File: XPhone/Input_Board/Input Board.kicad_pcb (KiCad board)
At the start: 2 copper layers, 100 x 100 mm, 94 parts, among them J1 AUDIO, J10 ENV, J11 PULSE, J12 PULSE, J13 Power In, J14 Power Out, J2 AUDIO, J3 ENV, J4 ENV, J5 PULSE, J6 PULSE, J7 AUDIO, J8 AUDIO, J9 ENV, Q1 BC847CW, Q2 BC847CW, Q3 BC847CW, Q4 BC847CW, Q5 BC847CW, Q6 BC847CW, Q7 BC847CW, Q8 BC847CW, U1 LM833, U2 78L05, U3 TL084, U4 74HC14, U5 LM833

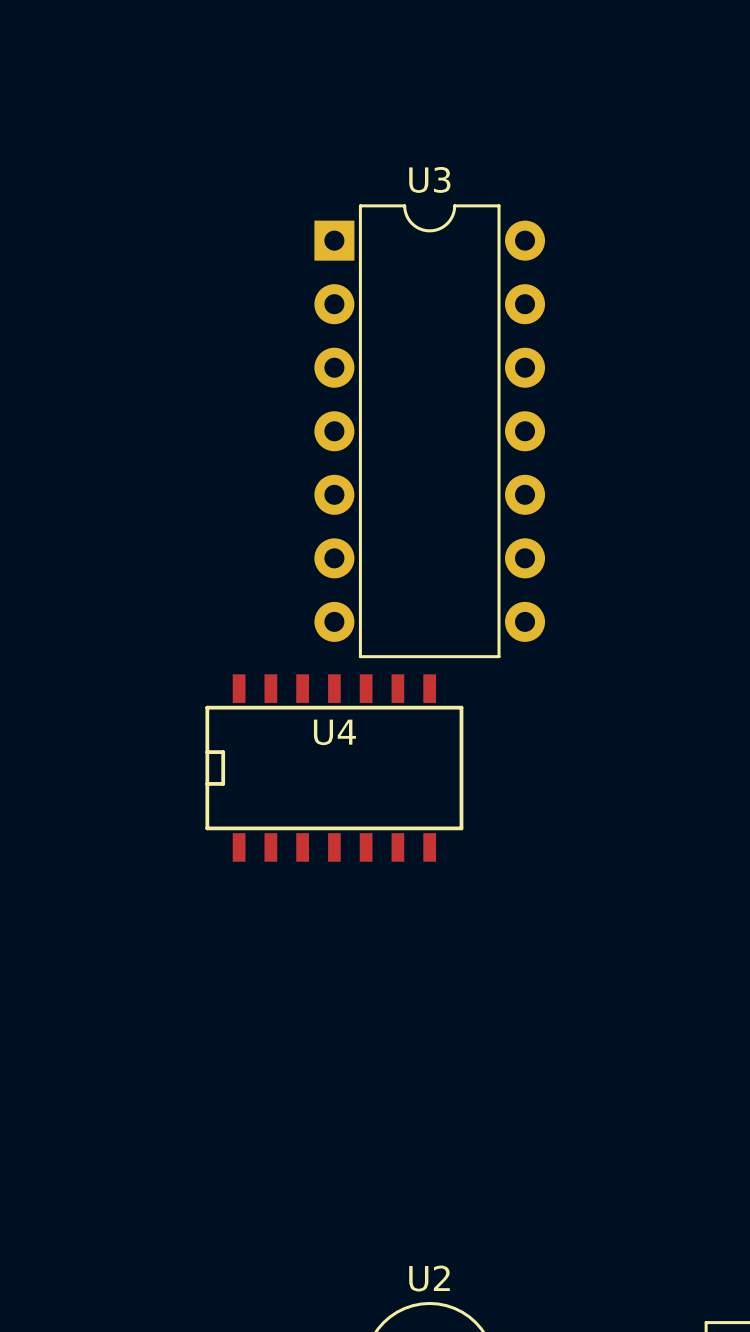
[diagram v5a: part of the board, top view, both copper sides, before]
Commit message: made tl084 a SOIC and returned 74hc14 back to a DIP
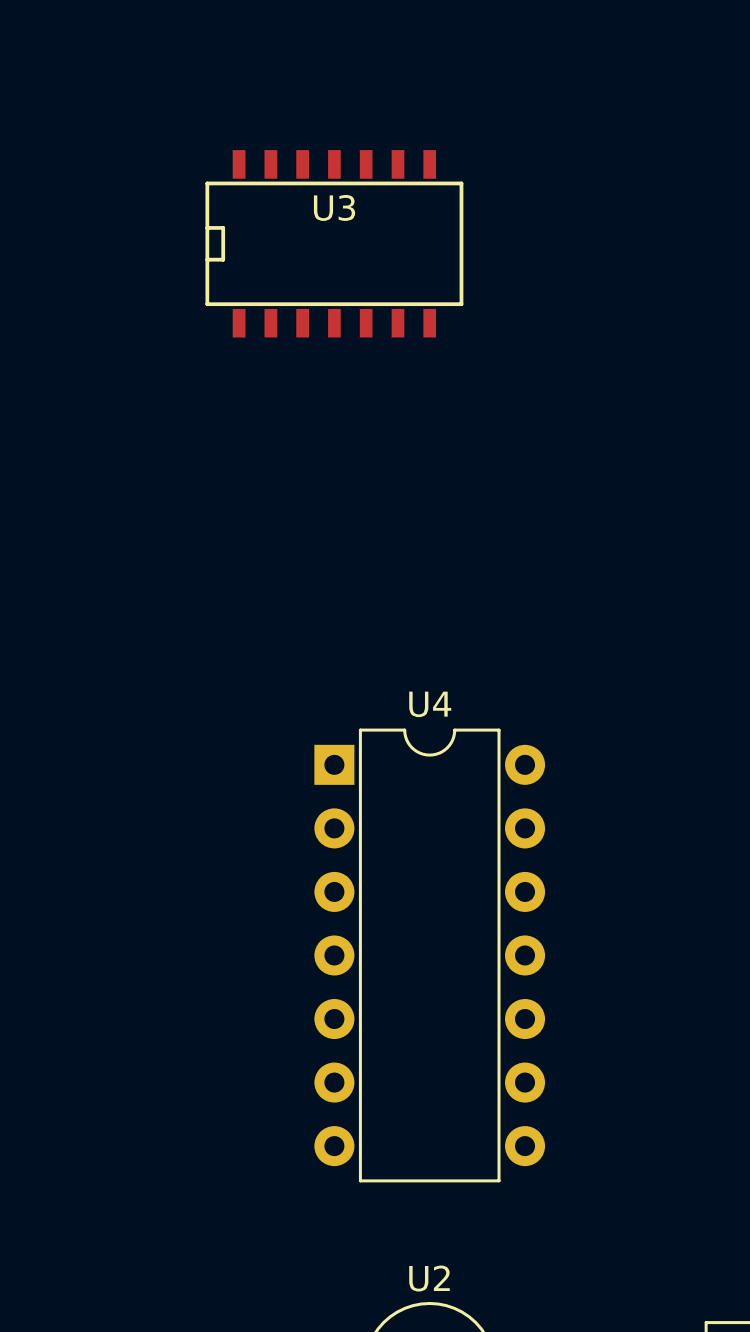
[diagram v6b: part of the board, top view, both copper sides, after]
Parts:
- U3: footprint Housings_DIP:DIP-14_W7.62mm -> SMD_Packages:SOIC-14_N
- U4: footprint SMD_Packages:SOIC-14_N -> Housings_DIP:DIP-14_W7.62mm

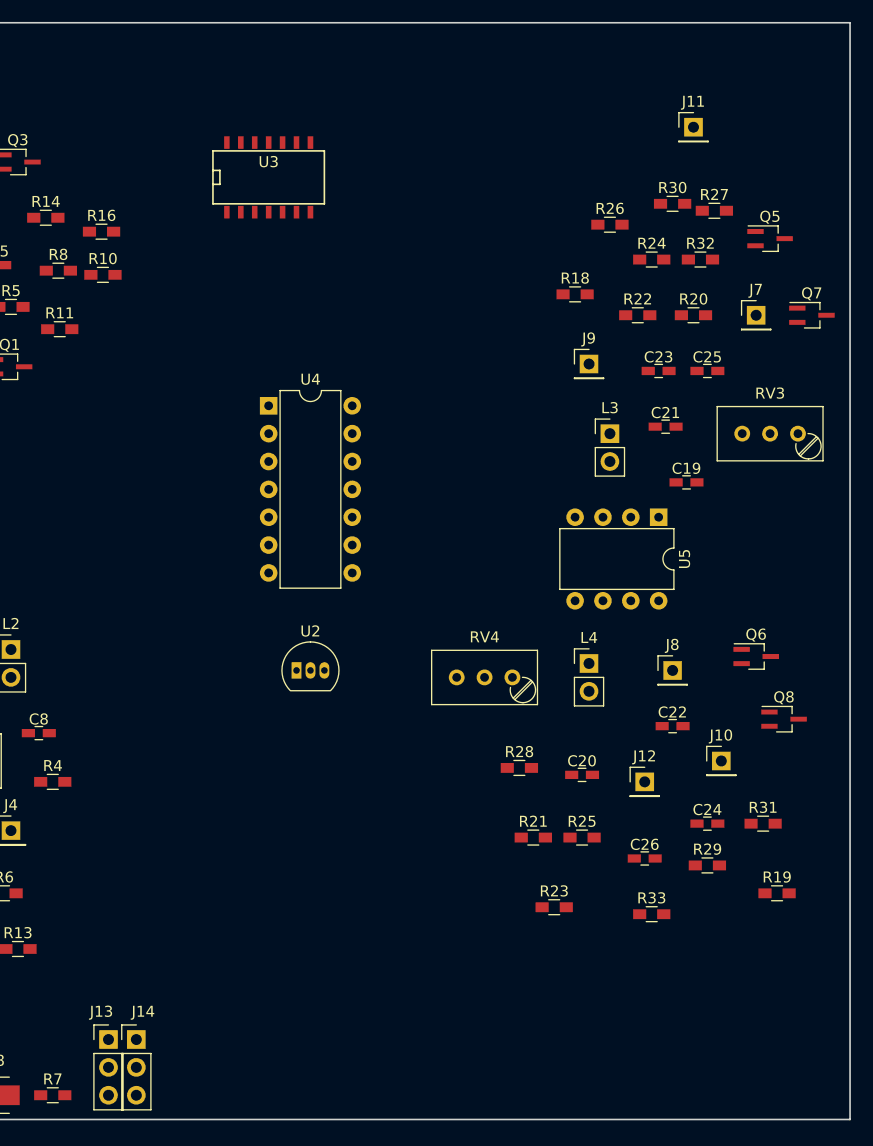
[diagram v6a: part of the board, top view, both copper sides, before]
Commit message: XPhone/Input_Board - placed parts around L3 amplifier
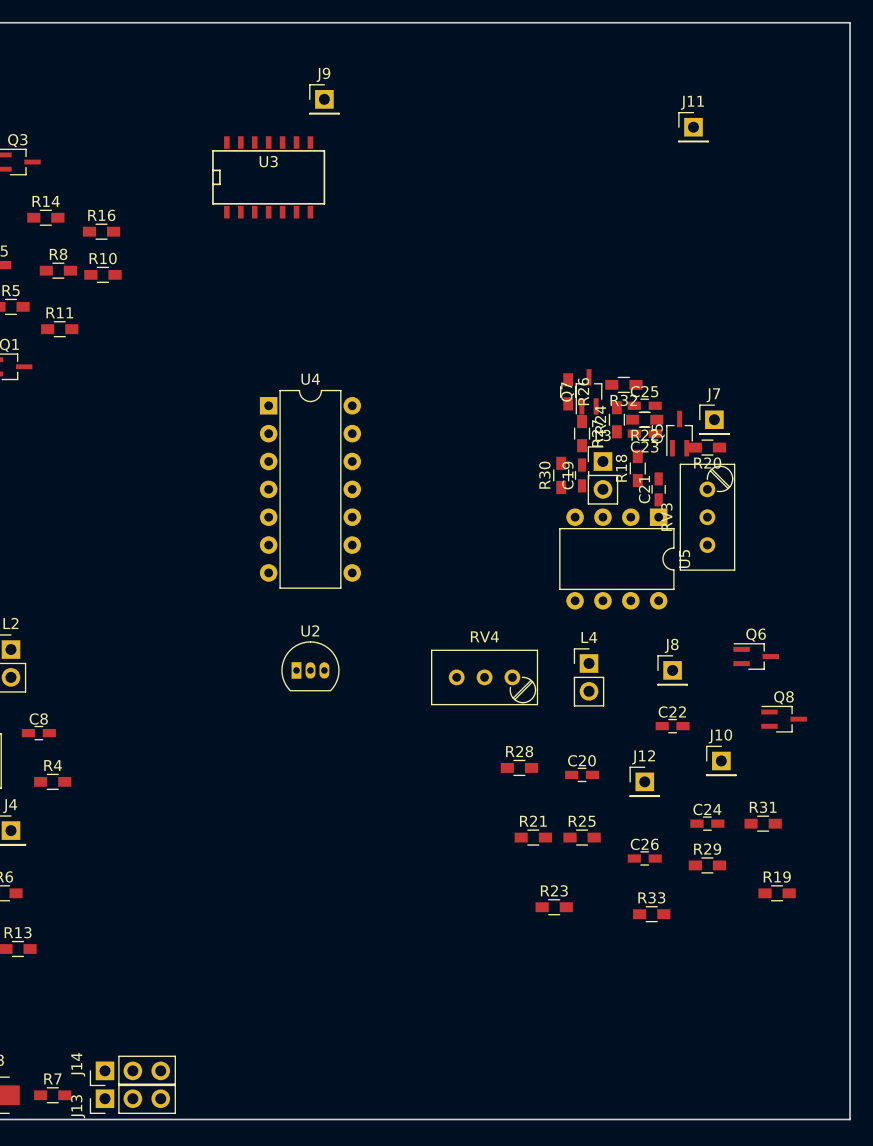
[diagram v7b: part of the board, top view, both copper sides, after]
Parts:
- moved J9 34.1 mm to (62.9, 17.8)
- moved R30 26.8 mm to (84.5, 52.1), turned to 90 degrees
- moved R27 23.6 mm to (86.4, 48.3), turned to 270 degrees
- moved Q7 21.5 mm to (87.0, 44.5), turned to 90 degrees
- moved Q5 19.6 mm to (95.2, 48.3), turned to 90 degrees
- moved R18 16.9 mm to (91.4, 51.4), turned to 90 degrees
- moved R26 15.7 mm to (85.1, 44.5), turned to 270 degrees
- moved R24 14.9 mm to (89.5, 47.0), turned to 90 degrees
- moved R32 13.4 mm to (90.2, 43.8), turned to 180 degrees
- moved R20 12.1 mm to (97.8, 49.5), turned to 180 degrees
- moved J7 10.3 mm to (98.4, 47.0)
- moved RV3 9.69 mm to (97.8, 53.3), turned to 90 degrees
- moved C19 9.55 mm to (86.4, 52.1), turned to 90 degrees
- moved R22 9.55 mm to (92.1, 47.0), turned to 180 degrees
- moved C25 6.54 mm to (92.1, 45.7)
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
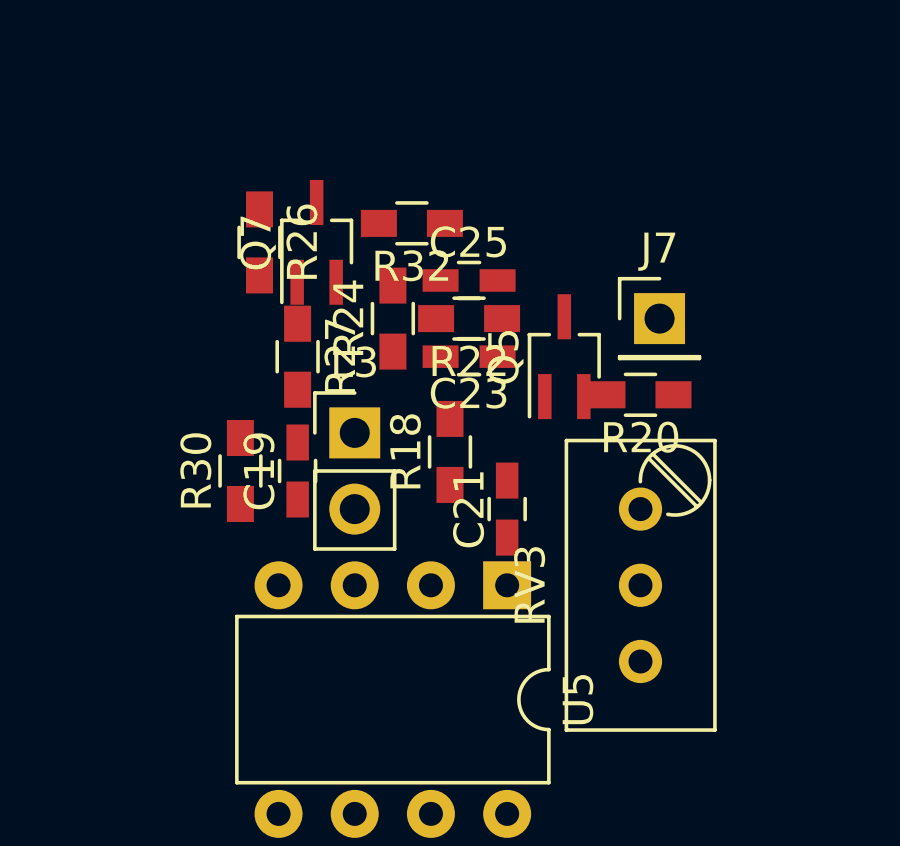
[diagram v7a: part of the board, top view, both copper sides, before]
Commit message: XPhone/Input_Board - laid traces for parts around L3
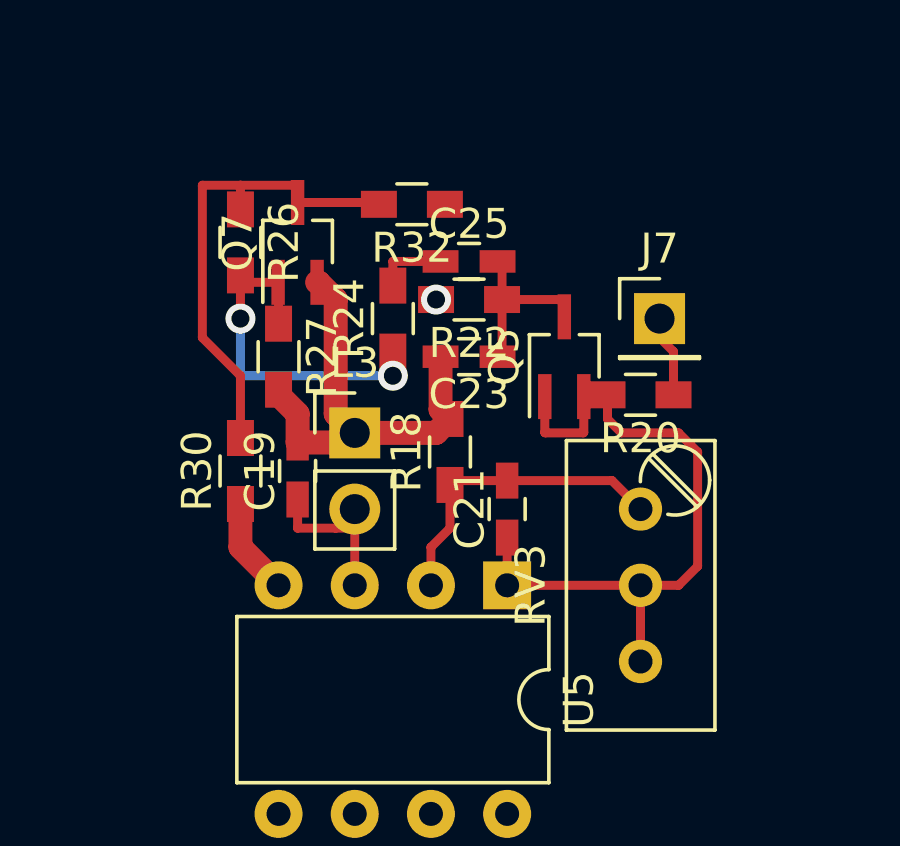
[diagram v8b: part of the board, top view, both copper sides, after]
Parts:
- moved Q7 0.64 mm to (86.4, 44.5)
- moved R22 0.64 mm to (92.1, 46.4)
- moved R26 0.64 mm to (84.5, 44.5)
- moved R27 0.64 mm to (85.7, 48.3)
- moved C25 0.63 mm to (92.1, 45.1)
- moved R32 0.63 mm to (90.2, 43.2)
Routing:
- net Net-(C21-Pad1): track 0.00 -> 23.3 mm
- net Net-(Q7-Pad3): track 0.00 -> 16.2 mm
- net GNDA: track 0.00 -> 15.2 mm
- net Net-(Q7-Pad1): track 0.00 -> 12.0 mm, vias 0 -> 2
- net Net-(C21-Pad2): track 0.00 -> 10.4 mm
- net Net-(C19-Pad1): track 0.00 -> 6.03 mm
- net Net-(C23-Pad1): track 0.00 -> 6.03 mm
- net +12V: track 0.00 -> 3.24 mm
- net Net-(J7-Pad1): track 0.00 -> 2.73 mm
- net Net-(C25-Pad1): track 0.00 -> 2.40 mm
- net V_ENV_BIAS: track 0.00 -> 0.17 mm, vias 0 -> 1
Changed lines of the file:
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@@
   (general
     (links 174)
-    (no_connects 174)
+    (no_connects 146)
     (area 10.719999 10.719999 111.315 113.11)
     (thickness 1.6)
     (drawings 4)
-    (tracks 0)
+    (tracks 77)
     (zones 0)
     (modules 94)
@@
     (pad_to_mask_clearance 0.2)
     (aux_axis_origin 0 0)
-    (visible_elements 7FFEFFFF)
+    (visible_elements 7FFEF7FF)
     (pcbplotparams
       (layerselection 0x00000_00000001)
@@
   )
   (module TO_SOT_Packages_SMD:SOT-323_SC-70_Handsoldering (layer F.Cu)
-    (at 86.995 44.45 90)
+    (at 86.36 44.45 90)
     (descr "SOT-323, SC-70 Handsoldering")
     (tags "SOT-323 SC-70 Handsoldering")
@@
   )
   (module Resistors_SMD:R_0603_HandSoldering (layer F.Cu)
-    (at 90.17 43.815 180)
+    (at 90.17 43.18 180)
     (descr "Resistor SMD 0603, hand soldering")
     (tags "resistor 0603")
@@
   )
   (module Resistors_SMD:R_0603_HandSoldering (layer F.Cu)
-    (at 86.36 48.26 270)
+    (at 85.725 48.26 270)
     (descr "Resistor SMD 0603, hand soldering")
     (tags "resistor 0603")
@@
   )
   (module Resistors_SMD:R_0603_HandSoldering (layer F.Cu)
-    (at 85.09 44.45 270)
+    (at 84.455 44.45 270)
     (descr "Resistor SMD 0603, hand soldering")
     (tags "resistor 0603")
@@
   )
   (module Resistors_SMD:R_0603_HandSoldering (layer F.Cu)
-    (at 92.075 46.99 180)
+    (at 92.075 46.355 180)
     (descr "Resistor SMD 0603, hand soldering")
     (tags "resistor 0603")
@@
   )
   (module Capacitors_SMD:C_0603_HandSoldering (layer F.Cu)
-    (at 92.075 45.72)
+    (at 92.075 45.085)
     (descr "Capacitor SMD 0603, hand soldering")
     (tags "capacitor 0603")
@@
   (gr_line (start 110.795 10.795) (end 110.795 110.795) (angle 90) (layer Edge.Cuts) (width 0.15))
   (gr_line (start 10.795 10.795) (end 110.795 10.795) (angle 90) (layer Edge.Cuts) (width 0.15))
+  (segment (start 85.725 55.88) (end 84.455 54.61) (width 0.8) (layer F.Cu) (net 1) (status 400000))
+  (segment (start 84.455 54.61) (end 84.455 53.17) (width 0.8) (layer F.Cu) (net 1) (status 800000))
+  (segment (start 91.125 48.26) (end 91.125 50.02) (width 0.8) (layer F.Cu) (net 3) (status C00000))
+  (segment (start 91.125 50.02) (end 91.44 50.335) (width 0.8) (layer F.Cu) (net 3) (status C00000))
+  (segment (start 87.01 45.78) (end 87.055 45.78) (width 0.8) (layer F.Cu) (net 3))
+  (segment (start 87.055 45.78) (end 87.63 46.355) (width 0.8) (layer F.Cu) (net 3))
+  (segment (start 87.63 46.355) (end 87.63 50.165) (width 0.8) (layer F.Cu) (net 3))
+  (segment (start 87.63 50.165) (end 88.265 50.8) (width 0.8) (layer F.Cu) (net 3))
+  (segment (start 85.725 49.36) (end 85.725 49.53) (width 0.8) (layer F.Cu) (net 3))
+  (segment (start 85.725 49.53) (end 86.36 50.165) (width 0.8) (layer F.Cu) (net 3))
+  (segment (start 86.36 50.165) (end 86.36 51.12) (width 0.8) (layer F.Cu) (net 3))
+  (segment (start 86.36 51.12) (end 87.945 51.12) (width 0.8) (layer F.Cu) (net 3))
+  (segment (start 87.945 51.12) (end 88.265 50.8) (width 0.8) (layer F.Cu) (net 3))
+  (segment (start 88.265 50.8) (end 90.975 50.8) (width 0.8) (layer F.Cu) (net 3))
+  (segment (start 90.975 50.8) (end 91.44 50.335) (width 0.8) (layer F.Cu) (net 3))
+  (segment (start 86.36 53.02) (end 86.36 53.975) (width 0.3) (layer F.Cu) (net 15))
+  (segment (start 87.63 53.975) (end 88.265 53.975) (width 0.3) (layer F.Cu) (net 15))
+  (segment (start 86.36 53.975) (end 87.63 53.975) (width 0.3) (layer F.Cu) (net 15))
+  (segment (start 88.265 53.975) (end 88.265 53.34) (width 0.3) (layer F.Cu) (net 15))
+  (segment (start 88.265 55.88) (end 88.265 53.34) (width 0.3) (layer F.Cu) (net 15))
+  (segment (start 96.69 49.53) (end 96.69 50.335) (width 0.3) (layer F.Cu) (net 17))
+  (segment (start 99.06 55.88) (end 97.79 55.88) (width 0.3) (layer F.Cu) (net 17))
+  (segment (start 99.695 55.245) (end 99.06 55.88) (width 0.3) (layer F.Cu) (net 17))
+  (segment (start 99.695 51.435) (end 99.695 55.245) (width 0.3) (layer F.Cu) (net 17))
+  (segment (start 99.06 50.8) (end 99.695 51.435) (width 0.3) (layer F.Cu) (net 17))
+  (segment (start 97.155 50.8) (end 99.06 50.8) (width 0.3) (layer F.Cu) (net 17))
+  (segment (start 96.69 50.335) (end 97.155 50.8) (width 0.3) (layer F.Cu) (net 17))
+  (segment (start 95.9 49.59) (end 96.63 49.59) (width 0.3) (layer F.Cu) (net 17))
+  (segment (start 96.63 49.59) (end 96.69 49.53) (width 0.3) (layer F.Cu) (net 17))
+  (segment (start 94.6 49.59) (end 94.6 50.785) (width 0.3) (layer F.Cu) (net 17))
+  (segment (start 95.9 50.785) (end 95.9 49.59) (width 0.3) (layer F.Cu) (net 17))
+  (segment (start 95.885 50.8) (end 95.9 50.785) (width 0.3) (layer F.Cu) (net 17))
+  (segment (start 94.615 50.8) (end 95.885 50.8) (width 0.3) (layer F.Cu) (net 17))
+  (segment (start 94.6 50.785) (end 94.615 50.8) (width 0.3) (layer F.Cu) (net 17))
+  (segment (start 93.345 55.88) (end 93.345 54.29) (width 0.3) (layer F.Cu) (net 17))
+  (segment (start 97.79 55.88) (end 93.345 55.88) (width 0.3) (layer F.Cu) (net 17))
+  (segment (start 97.79 55.88) (end 97.79 58.42) (width 0.3) (layer F.Cu) (net 17))
+  (segment (start 93.345 52.39) (end 96.84 52.39) (width 0.3) (layer F.Cu) (net 18))
+  (segment (start 96.84 52.39) (end 97.79 53.34) (width 0.3) (layer F.Cu) (net 18))
+  (segment (start 93.345 52.39) (end 91.585 52.39) (width 0.3) (layer F.Cu) (net 18))
+  (segment (start 91.585 52.39) (end 91.44 52.535) (width 0.3) (layer F.Cu) (net 18))
+  (segment (start 90.805 55.88) (end 90.805 54.61) (width 0.3) (layer F.Cu) (net 18))
+  (segment (start 91.44 53.975) (end 91.44 52.535) (width 0.3) (layer F.Cu) (net 18))
+  (segment (start 90.805 54.61) (end 91.44 53.975) (width 0.3) (layer F.Cu) (net 18))
+  (segment (start 93.175 46.355) (end 93.175 45.235) (width 0.3) (layer F.Cu) (net 21) (status C00000))
+  (segment (start 93.175 45.235) (end 93.025 45.085) (width 0.3) (layer F.Cu) (net 21) (status C00000))
+  (segment (start 93.175 46.355) (end 95.25 46.355) (width 0.3) (layer F.Cu) (net 21) (status C00000))
+  (segment (start 95.25 46.355) (end 95.25 46.93) (width 0.3) (layer F.Cu) (net 21) (status C00000))
+  (segment (start 93.175 46.355) (end 93.175 48.11) (width 0.3) (layer F.Cu) (net 21) (status 10))
+  (segment (start 93.175 48.11) (end 93.025 48.26) (width 0.3) (layer F.Cu) (net 21))
+  (segment (start 93.235 46.295) (end 93.175 46.355) (width 0.3) (layer F.Cu) (net 21) (status 30))
+  (segment (start 91.125 45.085) (end 89.535 45.085) (width 0.3) (layer F.Cu) (net 23) (status 400000))
+  (segment (start 89.535 45.085) (end 89.535 45.89) (width 0.3) (layer F.Cu) (net 23) (status 800000))
+  (segment (start 98.425 46.99) (end 98.425 47.625) (width 0.3) (layer F.Cu) (net 31))
+  (segment (start 98.425 47.625) (end 98.89 48.09) (width 0.3) (layer F.Cu) (net 31))
+  (segment (start 98.89 48.09) (end 98.89 49.53) (width 0.3) (layer F.Cu) (net 31))
+  (via (at 90.975 46.355) (size 1) (drill 0.6) (layers F.Cu B.Cu) (net 37) (status C00000))
+  (segment (start 90.975 46.355) (end 90.805 46.355) (width 0.3) (layer B.Cu) (net 37) (status 400000))
+  (segment (start 85.71 45.78) (end 84.685 45.78) (width 0.3) (layer F.Cu) (net 44))
+  (segment (start 84.685 45.78) (end 84.455 45.55) (width 0.3) (layer F.Cu) (net 44))
+  (segment (start 85.725 47.16) (end 85.725 45.795) (width 0.3) (layer F.Cu) (net 44))
+  (segment (start 85.725 45.795) (end 85.71 45.78) (width 0.3) (layer F.Cu) (net 44))
+  (segment (start 89.535 48.09) (end 89.535 48.895) (width 0.3) (layer F.Cu) (net 44) (status 10))
+  (segment (start 84.455 46.99) (end 84.455 45.55) (width 0.3) (layer F.Cu) (net 44))
+  (via (at 84.455 46.99) (size 1) (drill 0.6) (layers F.Cu B.Cu) (net 44))
+  (segment (start 84.455 48.895) (end 84.455 46.99) (width 0.3) (layer B.Cu) (net 44))
+  (segment (start 89.535 48.895) (end 84.455 48.895) (width 0.3) (layer B.Cu) (net 44))
+  (via (at 89.535 48.895) (size 1) (drill 0.6) (layers F.Cu B.Cu) (net 44))
+  (segment (start 84.455 50.97) (end 84.455 48.895) (width 0.3) (layer F.Cu) (net 46) (status 400000))
+  (segment (start 83.185 42.545) (end 84.455 42.545) (width 0.3) (layer F.Cu) (net 46))
+  (segment (start 83.185 47.625) (end 83.185 42.545) (width 0.3) (layer F.Cu) (net 46))
+  (segment (start 84.455 48.895) (end 83.185 47.625) (width 0.3) (layer F.Cu) (net 46))
+  (segment (start 86.36 43.12) (end 89.01 43.12) (width 0.3) (layer F.Cu) (net 46))
+  (segment (start 89.01 43.12) (end 89.07 43.18) (width 0.3) (layer F.Cu) (net 46))
+  (segment (start 84.455 43.35) (end 84.455 42.545) (width 0.3) (layer F.Cu) (net 46))
+  (segment (start 86.36 42.545) (end 86.36 43.12) (width 0.3) (layer F.Cu) (net 46))
+  (segment (start 84.455 42.545) (end 86.36 42.545) (width 0.3) (layer F.Cu) (net 46))
 )
